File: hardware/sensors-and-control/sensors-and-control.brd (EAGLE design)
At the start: 88 x 90 mm, 79 parts, among them IC1 STM32L496ZET6

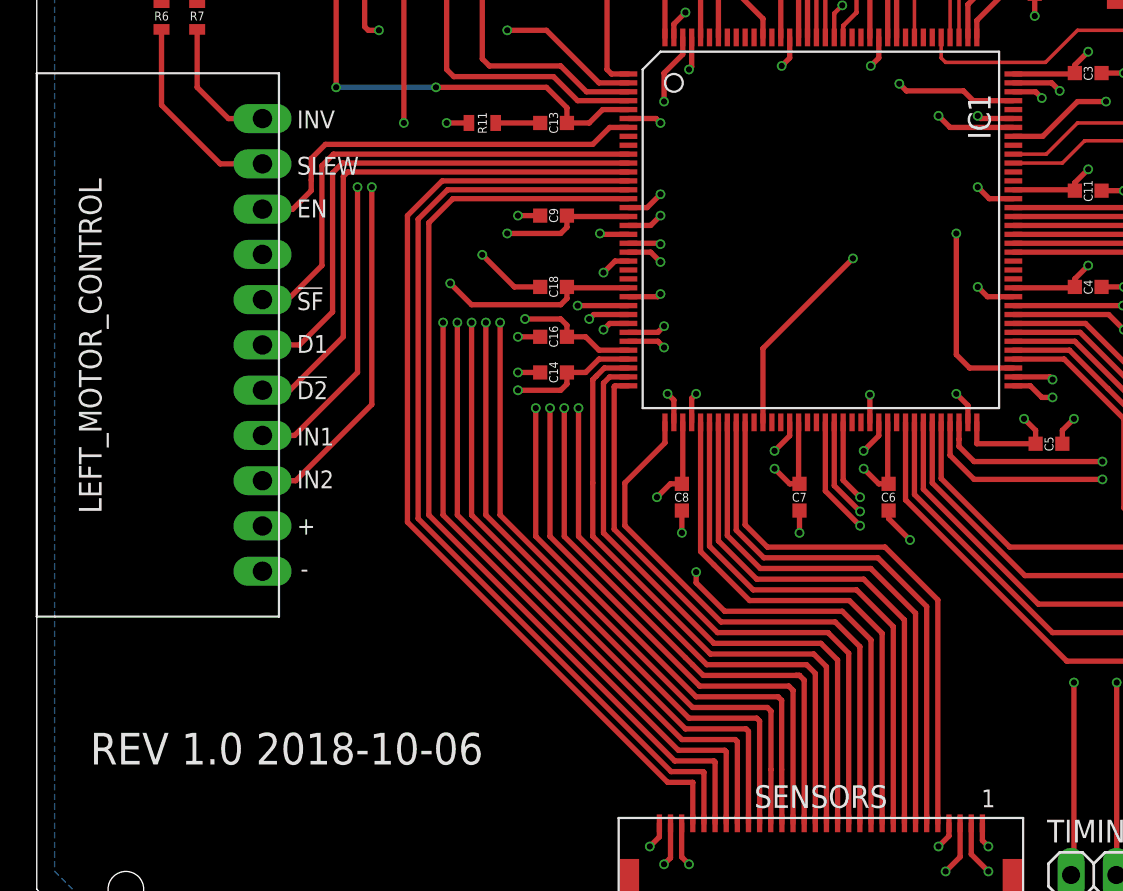
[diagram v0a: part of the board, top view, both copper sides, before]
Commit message: fixed flush button to use unused EXTI pin
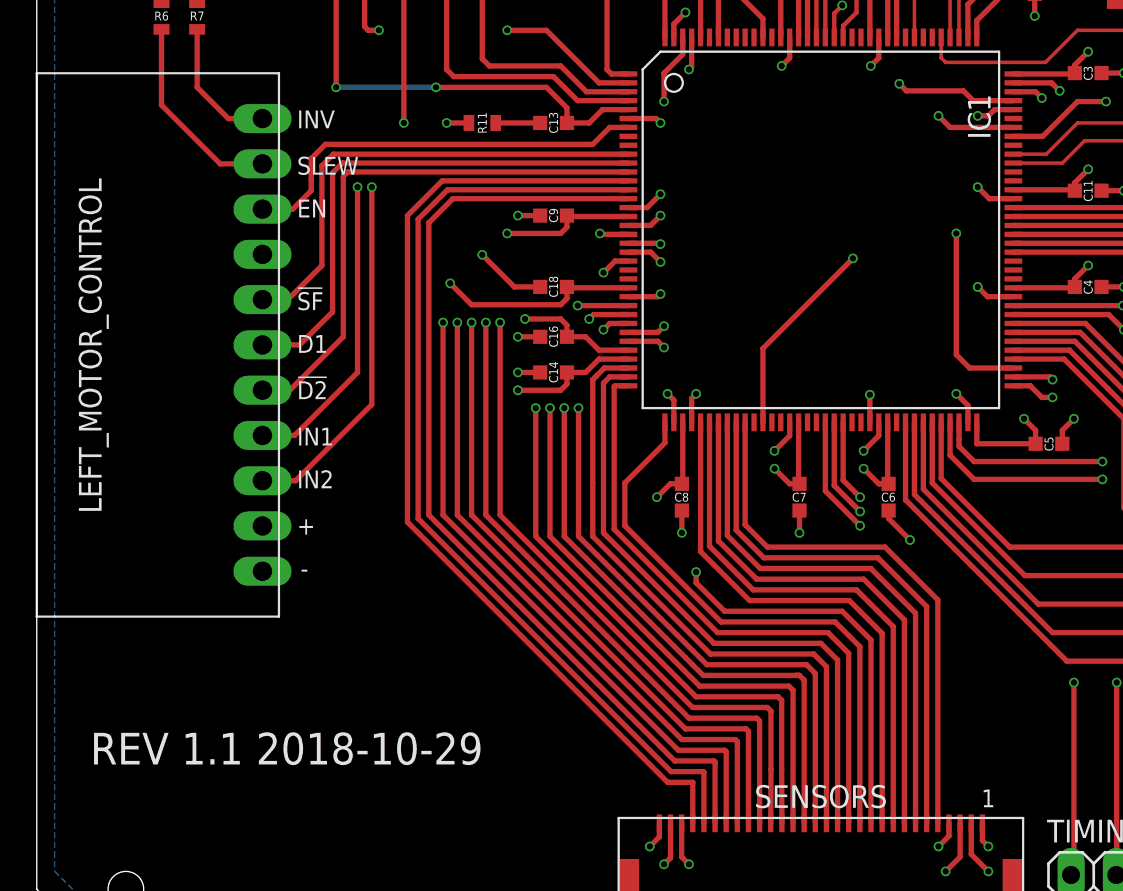
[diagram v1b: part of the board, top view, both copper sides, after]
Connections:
- net LM_ENC_OUT_A renamed LM_ENC_A
- net LM_ENC_OUT_B renamed LM_ENC_B
- net LM_PWM_IN1 renamed LM_PWM_1
- net LM_PWM_IN2 renamed LM_PWM_2
- net RM_ENC_OUT_A renamed RM_ENC_A
- net RM_ENC_OUT_B renamed RM_ENC_B
- net RM_PWM_IN1 renamed RM_PWM_1
- net RM_PWM_IN2 renamed RM_PWM_2
- removed net N$46: IC1.104
- new net N$30: IC1.103
- new net N$45: IC1.132
- net SD_FLUSH: now also IC1.104; no longer IC1.103
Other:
- board text added: "REV 1.1 2018-10-29"
- board text removed: "REV 1.0 2018-10-06"
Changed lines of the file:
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@@
 <drawing>
 <settings>
-<setting alwaysvectorfont="yes"/>
+<setting alwaysvectorfont="no"/>
 <setting verticaltext="up"/>
 </settings>
@@
 <text x="77.4" y="43" size="1" layer="26" rot="MR180" align="center-left">!SF</text>
 <text x="77.4" y="38" size="1" layer="26" rot="MR180" align="center-left">EN</text>
-<text x="3" y="22" size="1.778" layer="25">REV 1.0 2018-10-06</text>
+<text x="3" y="22" size="1.778" layer="25">REV 1.1 2018-10-29</text>
 <text x="14.6" y="55.6" size="1" layer="25" align="center-left">SLEW</text>
 <text x="14.6" y="58.2" size="1" layer="25" align="center-left">INV</text>
@@
 <wire x1="61.25" y1="81.8" x2="66.6" y2="81.8" width="0.2" layer="1"/>
 </signal>
-<signal name="RM_ENC_OUT_B">
+<signal name="RM_ENC_B">
 <contactref element="RIGHT_MOTOR_ENCODER" pad="2"/>
 <contactref element="IC1" pad="75"/>
@@
 <wire x1="63.515" y1="94.915" x2="60.4" y2="91.8" width="0.3" layer="2"/>
 </signal>
-<signal name="RM_ENC_OUT_A">
+<signal name="RM_ENC_A">
 <contactref element="RIGHT_MOTOR_ENCODER" pad="3"/>
 <contactref element="IC1" pad="81"/>
@@
 <wire x1="64.175" y1="92.375" x2="63.8" y2="92" width="0.3" layer="2"/>
 </signal>
-<signal name="LM_ENC_OUT_B">
+<signal name="LM_ENC_B">
 <contactref element="LEFT_MOTOR_ENCODER" pad="2"/>
 <contactref element="IC1" pad="2"/>
@@
 <wire x1="14.015" y1="92.385" x2="12.665" y2="92.375" width="0.3" layer="1"/>
 </signal>
-<signal name="LM_ENC_OUT_A">
+<signal name="LM_ENC_A">
 <contactref element="LEFT_MOTOR_ENCODER" pad="3"/>
 <contactref element="IC1" pad="60"/>
@@
 <wire x1="14.205" y1="43.005" x2="12.665" y2="43.005" width="0.3" layer="1"/>
 </signal>
-<signal name="LM_PWM_IN1">
+<signal name="LM_PWM_1">
 <contactref element="IC1" pad="141"/>
 <via x="18" y="54.4" extent="1-16" drill="0.35"/>
@@
 <wire x1="14.465" y1="40.465" x2="12.665" y2="40.465" width="0.3" layer="1"/>
 </signal>
-<signal name="LM_PWM_IN2">
+<signal name="LM_PWM_2">
 <contactref element="IC1" pad="142"/>
 <via x="18.8" y="54.4" extent="1-16" drill="0.35"/>
@@
 <wire x1="74.285" y1="48.085" x2="75.335" y2="48.085" width="0.3" layer="2"/>
 </signal>
-<signal name="RM_PWM_IN1">
+<signal name="RM_PWM_1">
 <contactref element="IC1" pad="48"/>
 <wire x1="40.75" y1="41.2" x2="40.75" y2="45.35" width="0.3" layer="1"/>
@@
 <wire x1="74.96" y1="51" x2="75.335" y2="50.625" width="0.3" layer="1"/>
 </signal>
-<signal name="RM_PWM_IN2">
+<signal name="RM_PWM_2">
 <contactref element="IC1" pad="82"/>
 <wire x1="54.8" y1="47.75" x2="60.95" y2="47.75" width="0.3" layer="1"/>
@@
 <contactref element="IC1" pad="100"/>
 </signal>
-<signal name="N$46">
-<contactref element="IC1" pad="104"/>
-</signal>
 <signal name="N$47">
 <contactref element="IC1" pad="137"/>
@@
 <contactref element="R26" pad="P$1"/>
 <contactref element="C15" pad="1"/>
-<contactref element="IC1" pad="103"/>
-<wire x1="54.8" y1="58.25" x2="52.95" y2="58.25" width="0.3" layer="1"/>
-<wire x1="52.95" y1="58.25" x2="52.8" y2="58.4" width="0.3" layer="1"/>
-<via x="52.8" y="58.4" extent="1-16" drill="0.35"/>
-<wire x1="52.8" y1="58.4" x2="52.8" y2="60.8" width="0.3" layer="2"/>
-<wire x1="52.8" y1="60.8" x2="56" y2="64" width="0.3" layer="2"/>
+<wire x1="56" y1="64" x2="52.8" y2="60.8" width="0.3" layer="2"/>
 <wire x1="56" y1="65.25" x2="56" y2="64" width="0.3" layer="1"/>
 <via x="56" y="64" extent="1-16" drill="0.35"/>
@@
 <wire x1="60.75" y1="74.55" x2="60.75" y2="65.45" width="0.3" layer="1"/>
 <wire x1="60.75" y1="65.45" x2="60.65" y2="65.35" width="0.3" layer="1"/>
+<contactref element="IC1" pad="104"/>
+<via x="52.8" y="58.4" extent="1-16" drill="0.35"/>
+<wire x1="52.8" y1="58.4" x2="53.4" y2="58.4" width="0.3" layer="1"/>
+<wire x1="53.4" y1="58.4" x2="53.75" y2="58.75" width="0.3" layer="1"/>
+<wire x1="53.75" y1="58.75" x2="54.8" y2="58.75" width="0.3" layer="1"/>
+<wire x1="52.8" y1="60.8" x2="52.8" y2="58.4" width="0.3" layer="2"/>
 </signal>
 <signal name="N$53">
@@
 <wire x1="57.8" y1="84.8" x2="64.05" y2="84.8" width="0.3" layer="1"/>
 </signal>
+<signal name="N$30">
+<contactref element="IC1" pad="103"/>
+</signal>
+<signal name="N$45">
+<contactref element="IC1" pad="132"/>
+</signal>
 </signals>
